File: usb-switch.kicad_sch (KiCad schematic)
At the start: 16 parts, among them IC1 MAX20337AEFT+T, IC2 MAX20337AEFT+T, IC3 MAX20337AEFT+T, IC4 MAX20337AEFT+T, IC5 TS3USB221ERSER, J1 DX07P024AJ1R1500, J2 Conn_01x05_Pin, J3 Conn_01x05_Pin, U1 74LVC1GU04DRL, U2 74LVC1GU04DRL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

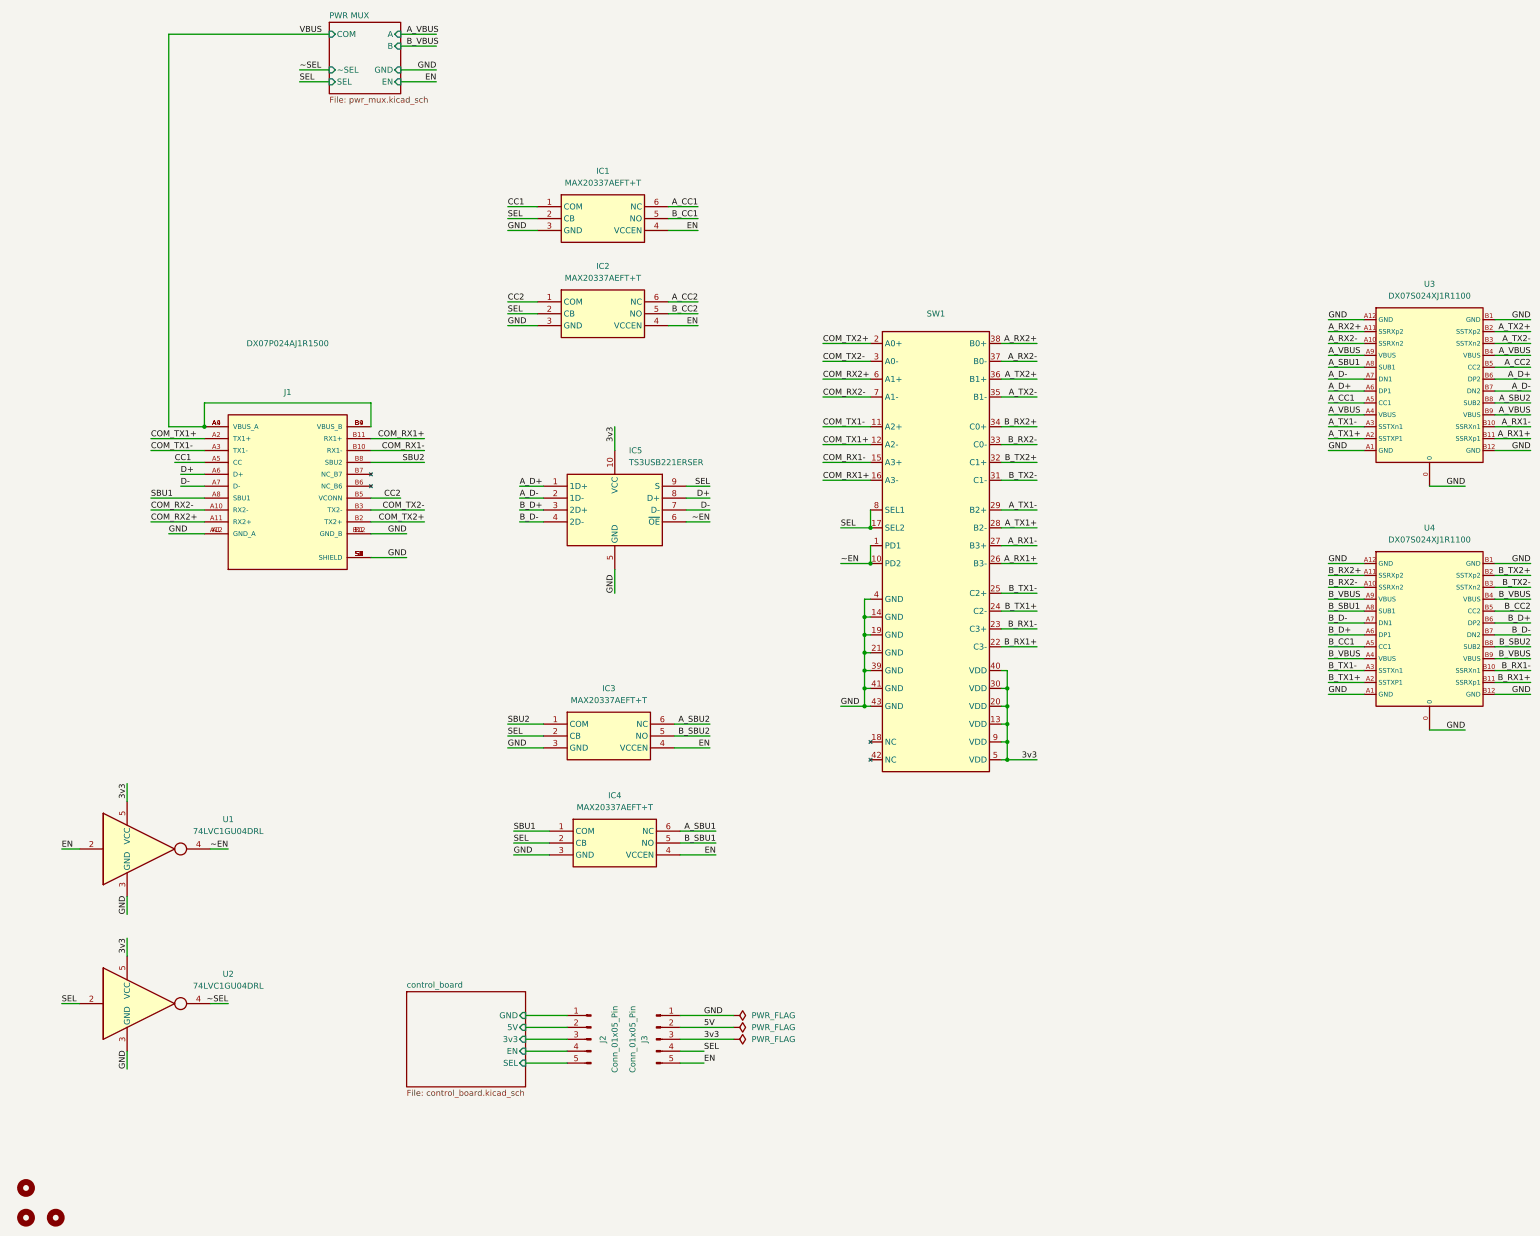
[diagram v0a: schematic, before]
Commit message: add capacitors, move B pwr control, select remaining components
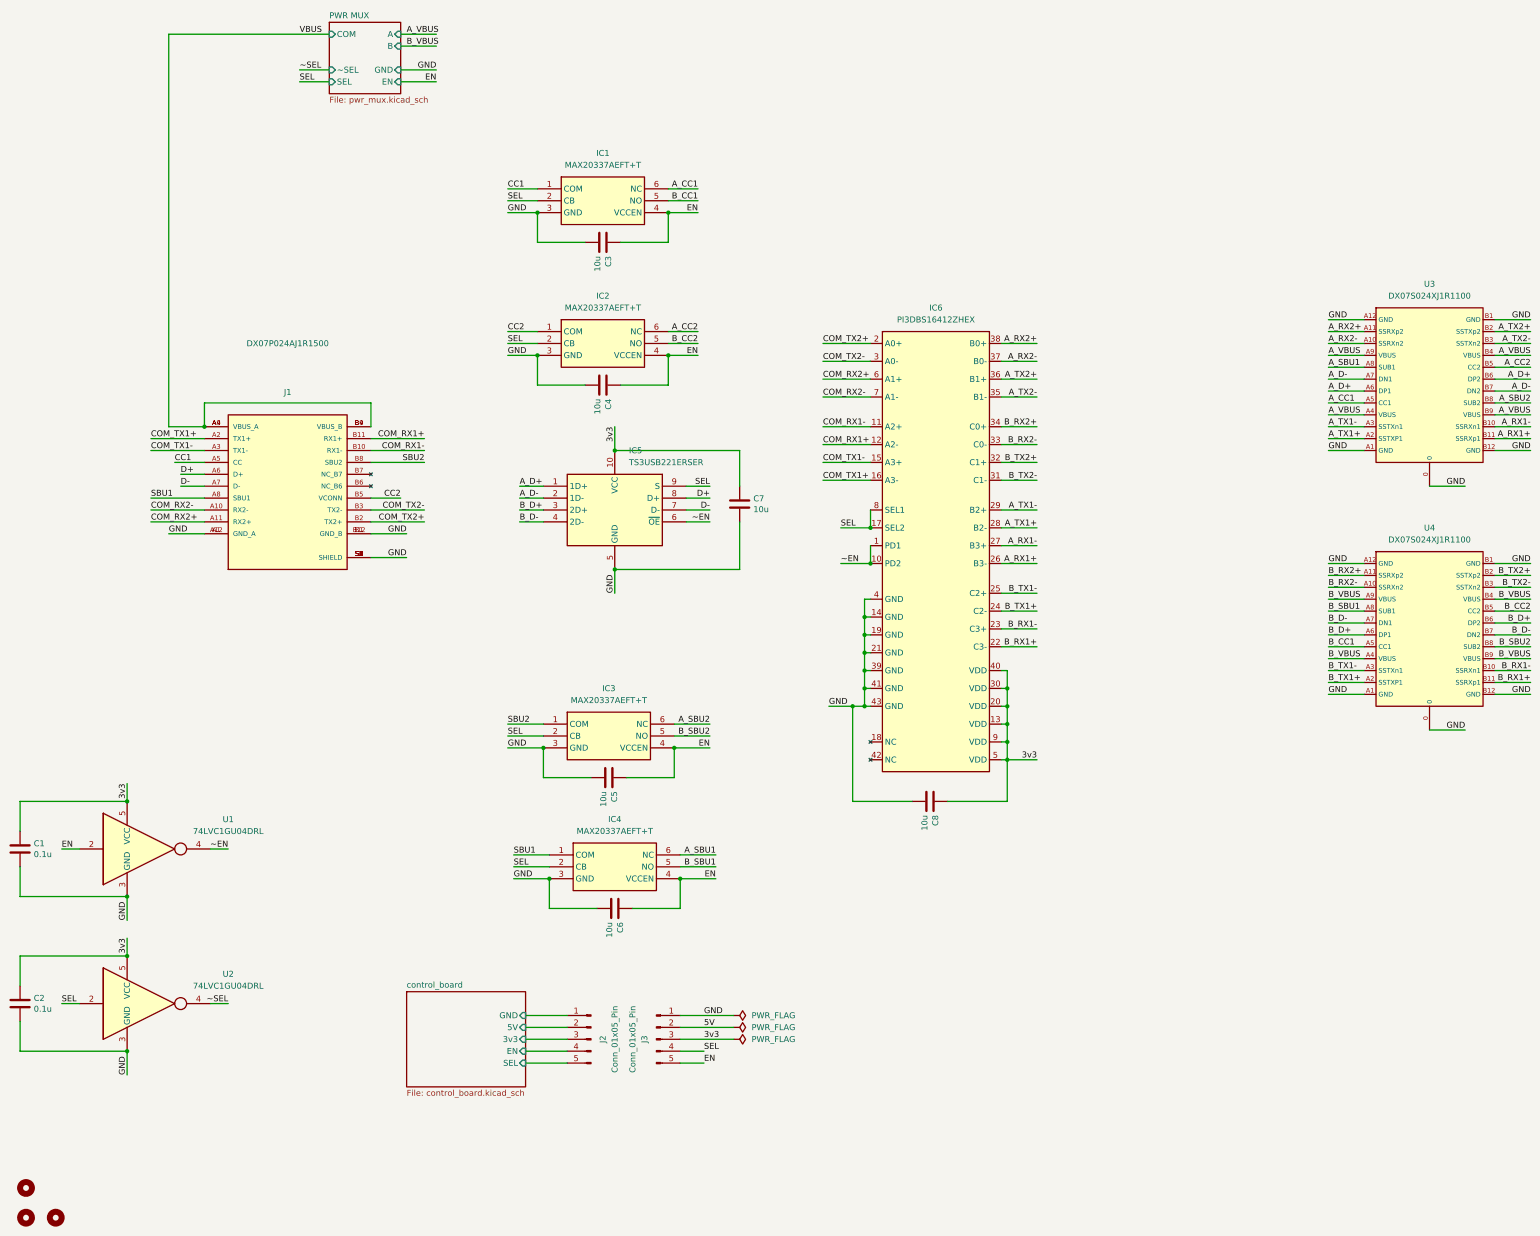
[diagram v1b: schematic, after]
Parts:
- added C1, C2: 0.1u, Capacitor_SMD:C_0402_1005Metric, symbol Device:C
- added C3, C4, C5, C6, C7, C8: 10u, Capacitor_SMD:C_0402_1005Metric, symbol Device:C
- IC6: renamed from SW1; value ~ -> PI3DBS16412ZHEX
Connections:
- net 3v3: now also C1.1, C2.1, C7.1, C8.1
- net COM_RX1+: now also IC6.12 (A2-); no longer IC6.16 (A3-)
- net COM_RX1-: now also IC6.11 (A2+); no longer IC6.15 (A3+)
- net COM_TX1+: now also IC6.16 (A3-); no longer IC6.12 (A2-)
- net COM_TX1-: now also IC6.15 (A3+); no longer IC6.11 (A2+)
- net EN: now also C3.1, C4.1, C5.1, C6.1
- net GND: now also C1.2, C2.2, C3.2, C4.2, C5.2, C6.2, C7.2, C8.2
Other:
- moved on the sheet: IC1, IC2, IC4

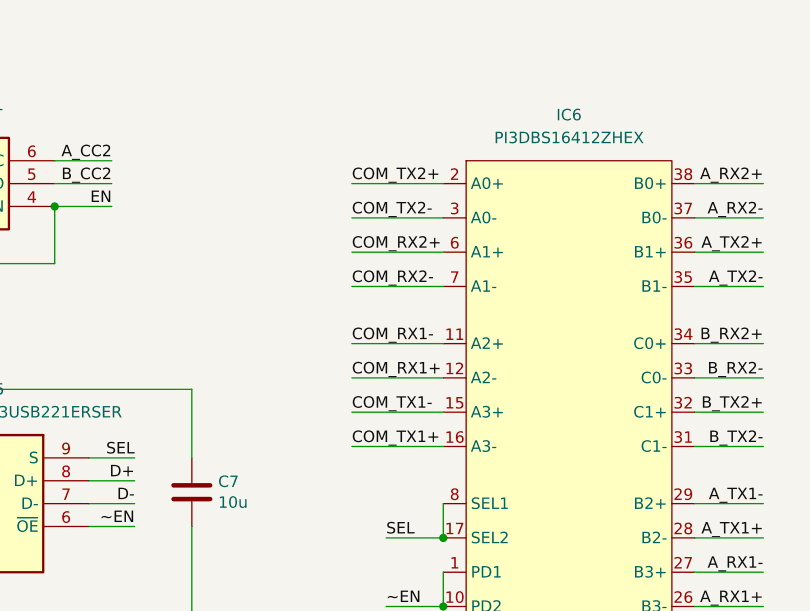
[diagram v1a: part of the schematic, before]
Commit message: fix usb connections, board dimensions
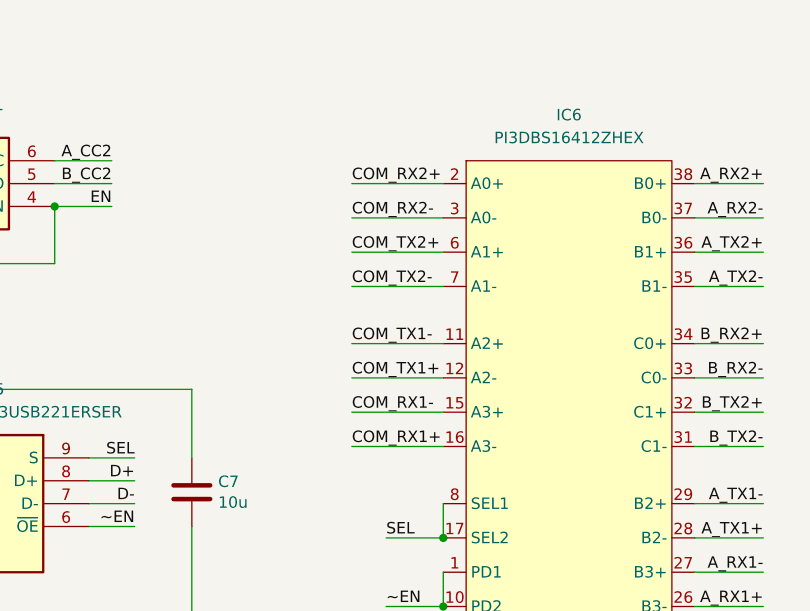
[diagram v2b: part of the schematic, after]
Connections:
- net COM_RX1+: now also IC6.16 (A3-); no longer IC6.12 (A2-)
- net COM_RX1-: now also IC6.15 (A3+); no longer IC6.11 (A2+)
- net COM_RX2+: now also IC6.2 (A0+); no longer IC6.6 (A1+)
- net COM_RX2-: now also IC6.3 (A0-); no longer IC6.7 (A1-)
- net COM_TX1+: now also IC6.12 (A2-); no longer IC6.16 (A3-)
- net COM_TX1-: now also IC6.11 (A2+); no longer IC6.15 (A3+)
- net COM_TX2+: now also IC6.6 (A1+); no longer IC6.2 (A0+)
- net COM_TX2-: now also IC6.7 (A1-); no longer IC6.3 (A0-)
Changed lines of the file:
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@@
 	(wire
 		(pts
-			(xy 189.23 110.49) (xy 199.39 110.49)
-		)
-		(stroke
-			(width 0)
-			(type default)
-		)
-	)
-	(wire
-		(pts
 			(xy 198.12 154.94) (xy 198.12 158.75)
 		)
@@
 	(wire
 		(pts
+			(xy 189.23 96.52) (xy 199.39 96.52)
+		)
+		(stroke
+			(width 0)
+			(type default)
+		)
+	)
+	(wire
+		(pts
 			(xy 17.78 243.84) (xy 17.78 237.49)
 		)
@@
 	(wire
 		(pts
-			(xy 189.23 118.11) (xy 199.39 118.11)
-		)
-		(stroke
-			(width 0)
-			(type default)
-		)
-	)
-	(wire
-		(pts
 			(xy 198.12 151.13) (xy 198.12 154.94)
 		)
@@
 	(wire
 		(pts
-			(xy 189.23 121.92) (xy 199.39 121.92)
-		)
-		(stroke
-			(width 0)
-			(type default)
-		)
-	)
-	(wire
-		(pts
 			(xy 128.27 64.77) (xy 121.92 64.77)
 		)
@@
 	(wire
 		(pts
-			(xy 189.23 100.33) (xy 199.39 100.33)
-		)
-		(stroke
-			(width 0)
-			(type default)
-		)
-	)
-	(wire
-		(pts
 			(xy 195.58 170.18) (xy 198.12 170.18)
 		)
@@
 	(wire
 		(pts
+			(xy 189.23 121.92) (xy 199.39 121.92)
+		)
+		(stroke
+			(width 0)
+			(type default)
+		)
+	)
+	(wire
+		(pts
 			(xy 128.27 101.6) (xy 138.43 101.6)
 		)
@@
 	(wire
 		(pts
-			(xy 189.23 104.14) (xy 199.39 104.14)
+			(xy 189.23 110.49) (xy 199.39 110.49)
 		)
 		(stroke
@@
 	(wire
 		(pts
-			(xy 189.23 114.3) (xy 199.39 114.3)
-		)
-		(stroke
-			(width 0)
-			(type default)
-		)
-	)
-	(wire
-		(pts
 			(xy 234.95 100.33) (xy 227.33 100.33)
 		)
@@
 	(wire
 		(pts
+			(xy 189.23 104.14) (xy 199.39 104.14)
+		)
+		(stroke
+			(width 0)
+			(type default)
+		)
+	)
+	(wire
+		(pts
 			(xy 17.78 196.85) (xy 17.78 190.5)
 		)
@@
 	(wire
 		(pts
+			(xy 189.23 114.3) (xy 199.39 114.3)
+		)
+		(stroke
+			(width 0)
+			(type default)
+		)
+	)
+	(wire
+		(pts
 			(xy 158.75 236.22) (xy 170.18 236.22)
 		)
@@
 	(wire
 		(pts
-			(xy 189.23 96.52) (xy 199.39 96.52)
+			(xy 189.23 118.11) (xy 199.39 118.11)
 		)
 		(stroke
@@
 	(wire
 		(pts
-			(xy 189.23 92.71) (xy 199.39 92.71)
-		)
-		(stroke
-			(width 0)
-			(type default)
-		)
-	)
-	(wire
-		(pts
 			(xy 128.27 95.25) (xy 121.92 95.25)
 		)
@@
 	(wire
 		(pts
+			(xy 189.23 100.33) (xy 199.39 100.33)
+		)
+		(stroke
+			(width 0)
+			(type default)
+		)
+	)
+	(wire
+		(pts
 			(xy 147.32 185.42) (xy 157.48 185.42)
 		)
@@
 	(wire
 		(pts
+			(xy 189.23 92.71) (xy 199.39 92.71)
+		)
+		(stroke
+			(width 0)
+			(type default)
+		)
+	)
+	(wire
+		(pts
 			(xy 332.74 95.25) (xy 340.36 95.25)
 		)
@@
 		)
 	)
+	(label "COM_RX2-"
+		(at 189.23 96.52 0)
+		(fields_autoplaced yes)
+		(effects
+			(font
+				(size 1.27 1.27)
+			)
+			(justify left bottom)
+		)
+	)
 	(label "B_RX1+"
 		(at 340.36 165.1 180)
@@
 		)
 	)
-	(label "SEL"
-		(at 193.04 132.08 0)
+	(label "COM_TX1-"
+		(at 189.23 110.49 0)
 		(fields_autoplaced yes)
 		(effects
@@
 		)
 	)
-	(label "COM_RX1-"
-		(at 189.23 110.49 0)
+	(label "SEL"
+		(at 193.04 132.08 0)
 		(fields_autoplaced yes)
 		(effects
@@
 		)
 	)
-	(label "COM_RX2+"
-		(at 189.23 100.33 0)
-		(fields_autoplaced yes)
-		(effects
-			(font
-				(size 1.27 1.27)
-			)
-			(justify left bottom)
-		)
-	)
 	(label "A_RX1-"
 		(at 234.95 135.89 180)
@@
 		)
 	)
+	(label "COM_RX1-"
+		(at 189.23 118.11 0)
+		(fields_autoplaced yes)
+		(effects
+			(font
+				(size 1.27 1.27)
+			)
+			(justify left bottom)
+		)
+	)
+	(label "COM_TX1+"
+		(at 189.23 114.3 0)
+		(fields_autoplaced yes)
+		(effects
+			(font
+				(size 1.27 1.27)
+			)
+			(justify left bottom)
+		)
+	)
 	(label "3v3"
 		(at 144.78 110.49 270)
@@
 		)
 	)
+	(label "COM_RX1+"
+		(at 189.23 121.92 0)
+		(fields_autoplaced yes)
+		(effects
+			(font
+				(size 1.27 1.27)
+			)
+			(justify left bottom)
+		)
+	)
 	(label "GND"
 		(at 100.33 138.43 180)
@@
 		)
 	)
-	(label "COM_RX2-"
-		(at 189.23 104.14 0)
-		(fields_autoplaced yes)
-		(effects
-			(font
-				(size 1.27 1.27)
-			)
-			(justify left bottom)
-		)
-	)
-	(label "COM_RX1+"
-		(at 189.23 114.3 0)
+	(label "B_CC1"
+		(at 297.18 157.48 0)
 		(fields_autoplaced yes)
 		(effects
@@
 		)
 	)
-	(label "B_CC1"
-		(at 297.18 157.48 0)
+	(label "COM_TX2-"
+		(at 189.23 104.14 0)
 		(fields_autoplaced yes)
 		(effects
@@
 		)
 	)
-	(label "SEL"
-		(at 165.1 123.19 180)
+	(label "COM_TX2+"
+		(at 189.23 100.33 0)
 		(fields_autoplaced yes)
 		(effects
@@
 				(size 1.27 1.27)
 			)
-			(justify right bottom)
+			(justify left bottom)
 		)
 	)
-	(label "COM_TX2-"
-		(at 189.23 96.52 0)
+	(label "SEL"
+		(at 165.1 123.19 180)
 		(fields_autoplaced yes)
 		(effects
@@
 				(size 1.27 1.27)
 			)
-			(justify left bottom)
+			(justify right bottom)
 		)
 	)
@@
 		)
 	)
-	(label "COM_TX1+"
-		(at 189.23 121.92 0)
-		(fields_autoplaced yes)
-		(effects
-			(font
-				(size 1.27 1.27)
-			)
-			(justify left bottom)
-		)
-	)
 	(label "A_VBUS"
 		(at 340.36 95.25 180)
@@
 		)
 	)
-	(label "COM_TX2+"
-		(at 189.23 92.71 0)
-		(fields_autoplaced yes)
-		(effects
-			(font
-				(size 1.27 1.27)
-			)
-			(justify left bottom)
-		)
-	)
 	(label "3v3"
 		(at 234.95 181.61 180)
@@
 		)
 	)
-	(label "COM_TX1-"
-		(at 189.23 118.11 0)
-		(fields_autoplaced yes)
-		(effects
-			(font
-				(size 1.27 1.27)
-			)
-			(justify left bottom)
-		)
-	)
 	(label "EN"
 		(at 162.56 95.25 180)
@@
 		(fields_autoplaced yes)
 		(effects
+			(font
+				(size 1.27 1.27)
+			)
+			(justify left bottom)
+		)
+	)
+	(label "COM_RX2+"
+		(at 189.23 92.71 0)
+		(fields_autoplaced yes)
+		(effects
